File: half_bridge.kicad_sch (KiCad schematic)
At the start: 19 parts

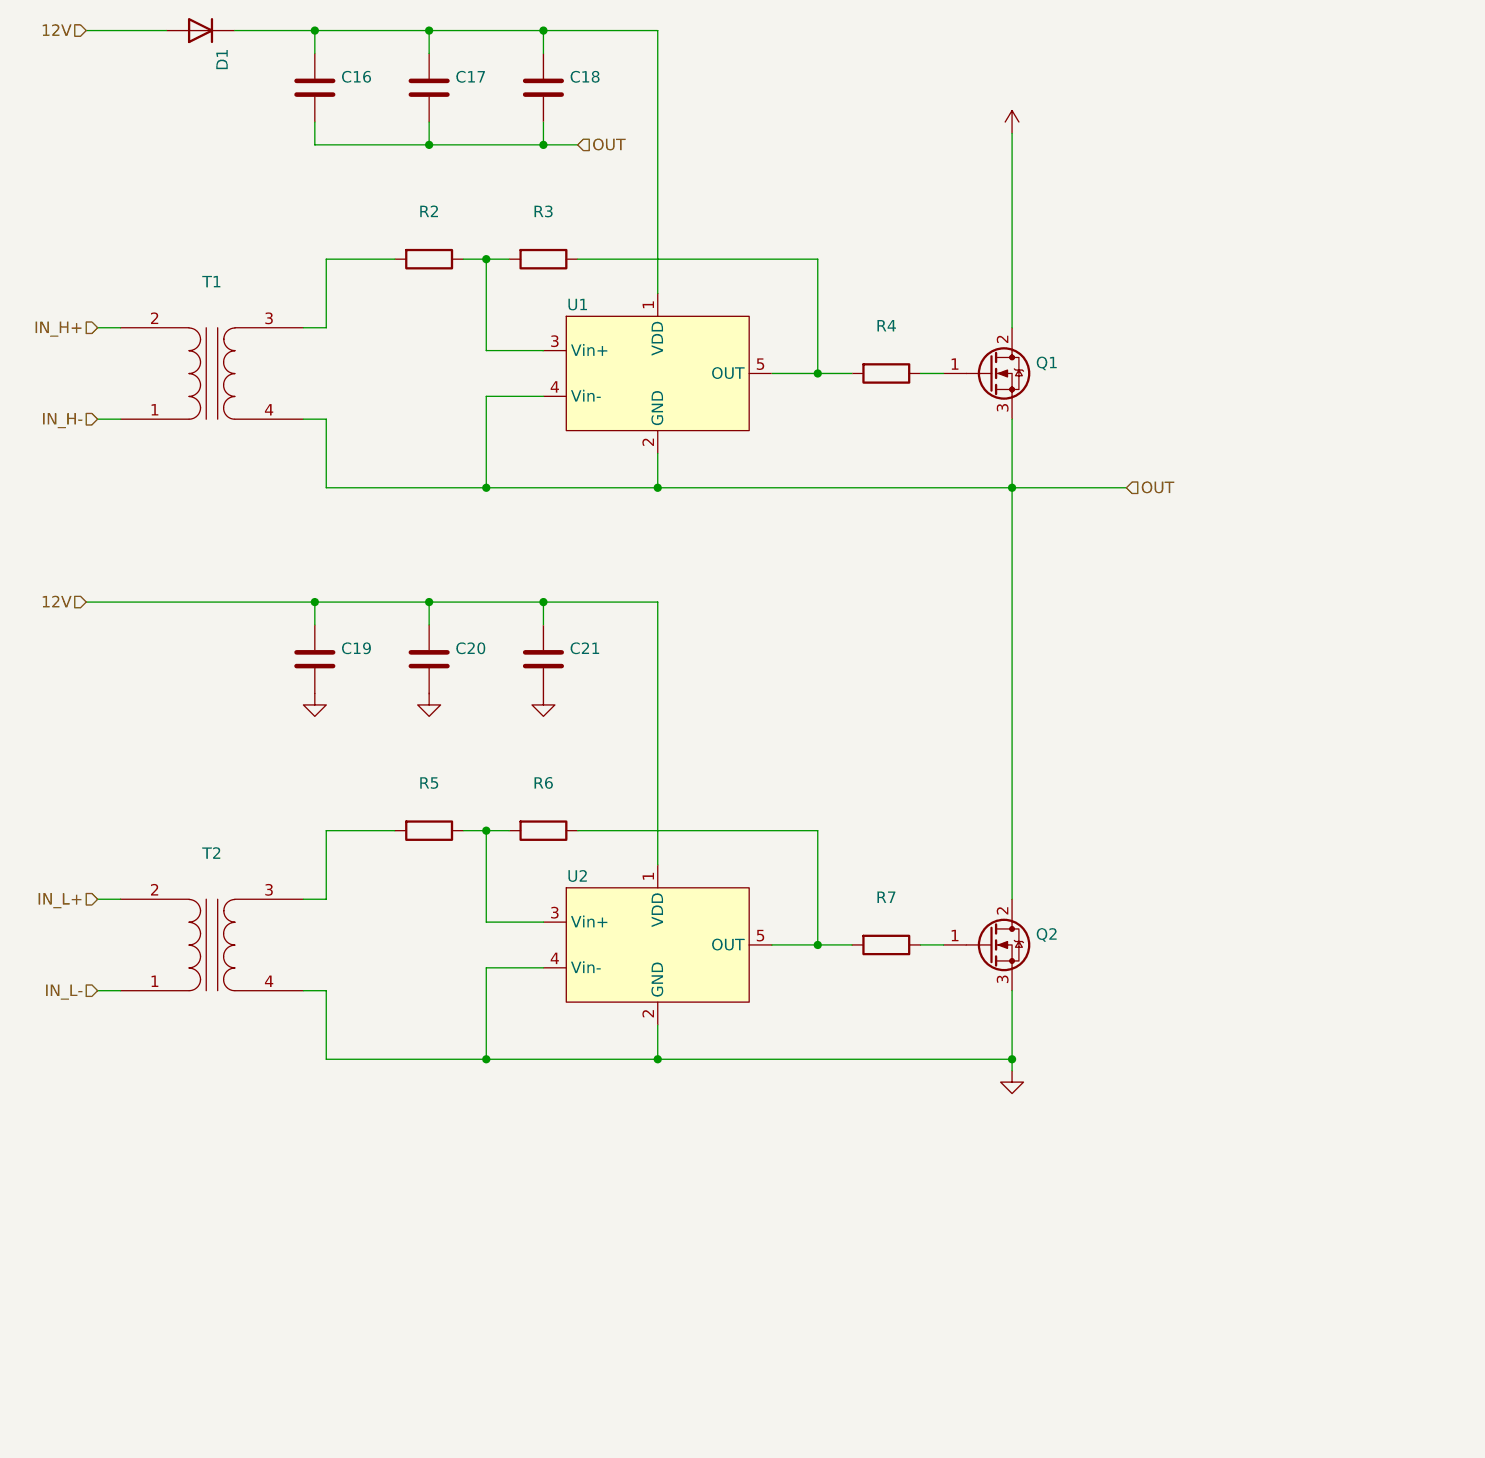
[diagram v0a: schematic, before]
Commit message: added/corrected placeholder resistor values
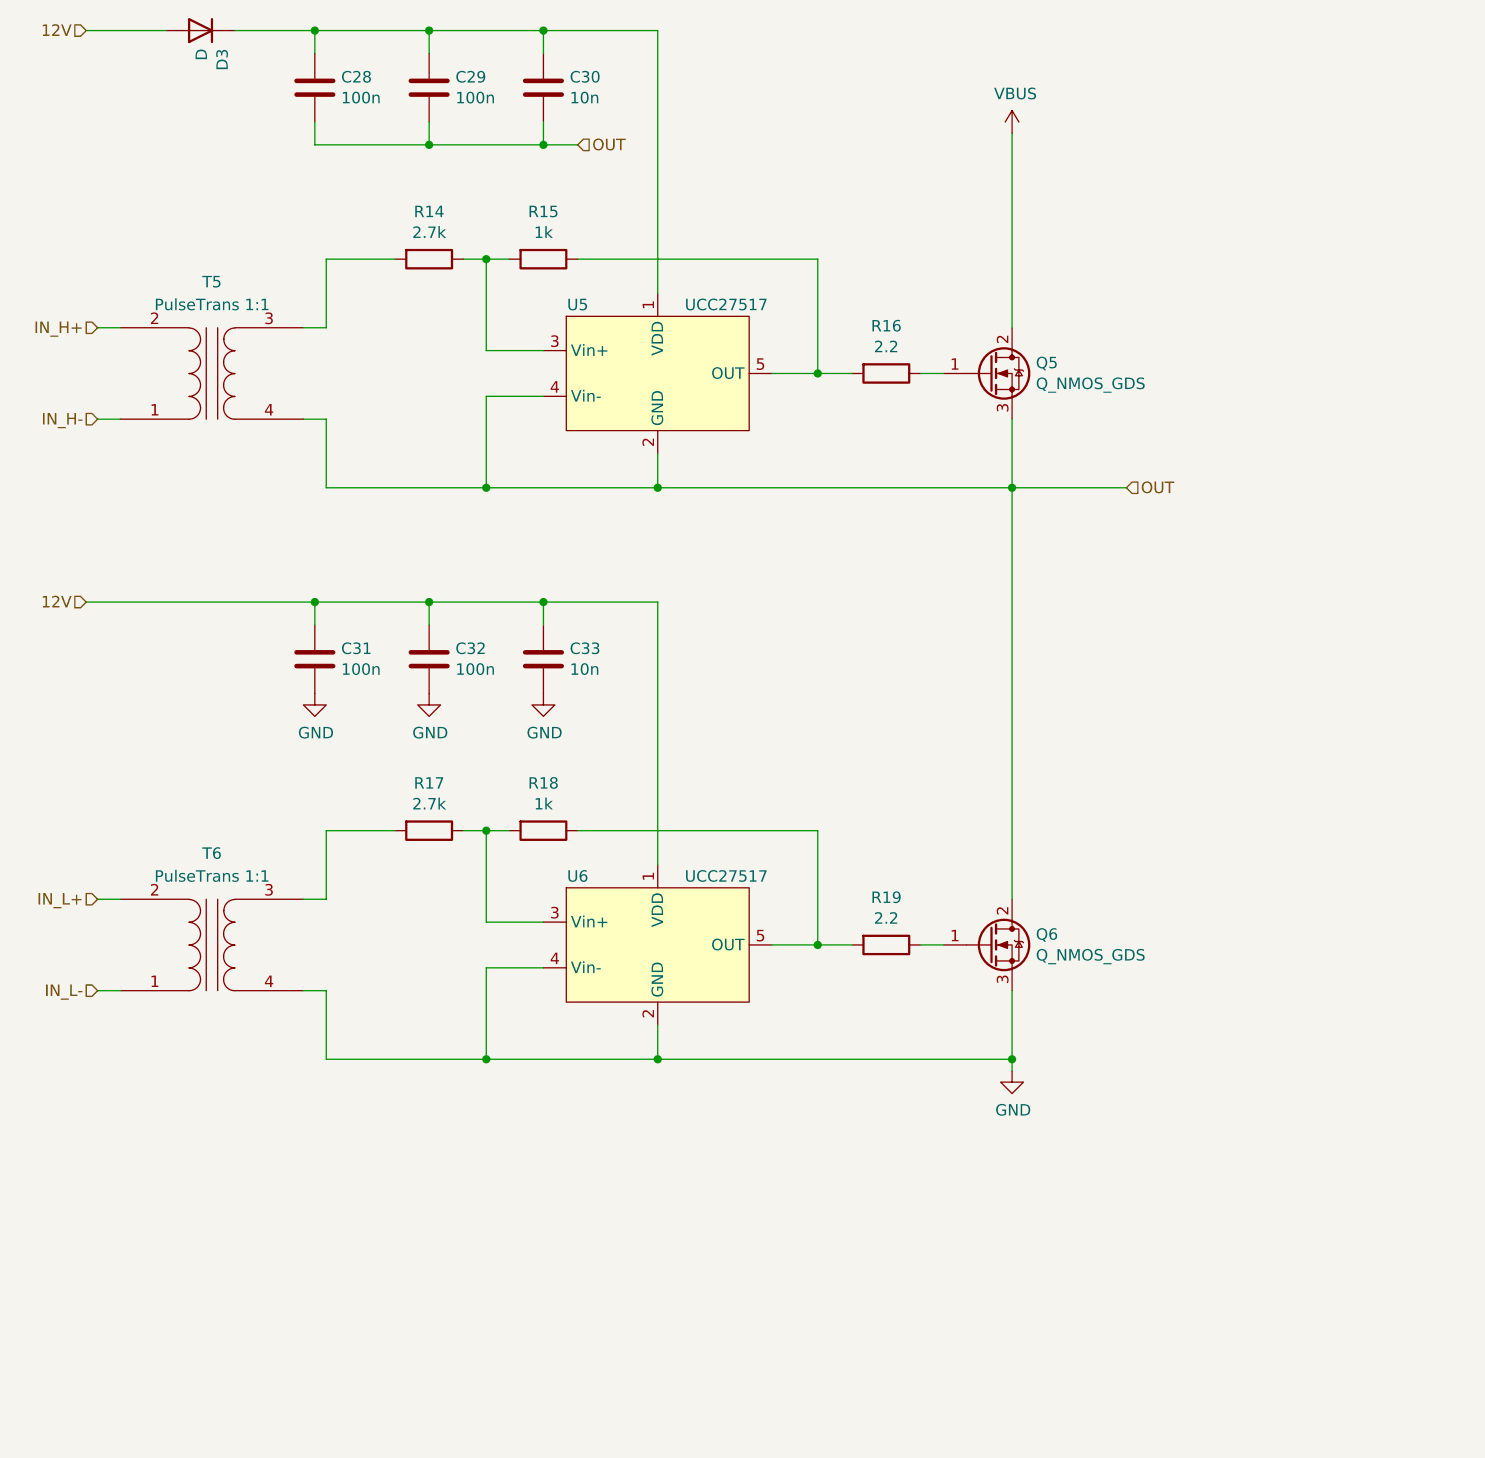
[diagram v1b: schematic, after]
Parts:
- C28: renamed from C16; value (none) -> 100n; footprint (none) -> Capacitor_SMD:C_0603_1608Metric
- C29: renamed from C17; value (none) -> 100n; footprint (none) -> Capacitor_SMD:C_0603_1608Metric
- C30: renamed from C18; value (none) -> 10n; footprint (none) -> Capacitor_SMD:C_0603_1608Metric
- C31: renamed from C19; value (none) -> 100n; footprint (none) -> Capacitor_SMD:C_0603_1608Metric
- C32: renamed from C20; value (none) -> 100n; footprint (none) -> Capacitor_SMD:C_0603_1608Metric
- C33: renamed from C21; value (none) -> 10n; footprint (none) -> Capacitor_SMD:C_0603_1608Metric
- D3: renamed from D1; value (none) -> D; footprint (none) -> Diode_SMD:D_SMA
- Q5: renamed from Q1; value (none) -> Q_NMOS_GDS; footprint (none) -> Package_TO_SOT_THT:TO-247-3_Horizontal_TabUp
- Q6: renamed from Q2; value (none) -> Q_NMOS_GDS; footprint (none) -> Package_TO_SOT_THT:TO-247-3_Horizontal_TabUp
- R14: renamed from R2; value (none) -> 2.7k; footprint (none) -> Resistor_SMD:R_0805_2012Metric
- R15: renamed from R3; value (none) -> 1k; footprint (none) -> Resistor_SMD:R_0805_2012Metric
- R16: renamed from R4; value (none) -> 2.2; footprint (none) -> Resistor_SMD:R_2512_6332Metric_Pad1.40x3.35mm_HandSolder
- R17: renamed from R5; value (none) -> 2.7k; footprint (none) -> Resistor_SMD:R_0805_2012Metric
- R18: renamed from R6; value (none) -> 1k; footprint (none) -> Resistor_SMD:R_0805_2012Metric
- R19: renamed from R7; value (none) -> 2.2; footprint (none) -> Resistor_SMD:R_2512_6332Metric_Pad1.40x3.35mm_HandSolder
- T5: renamed from T1; value (none) -> PulseTrans 1:1; footprint (none) -> universal-half-bridge:ESMIT-4180
- T6: renamed from T2; value (none) -> PulseTrans 1:1; footprint (none) -> universal-half-bridge:ESMIT-4180
- U5: renamed from U1; value (none) -> UCC27517; footprint (none) -> Package_TO_SOT_SMD:SOT-23-5
- U6: renamed from U2; value (none) -> UCC27517; footprint (none) -> Package_TO_SOT_SMD:SOT-23-5

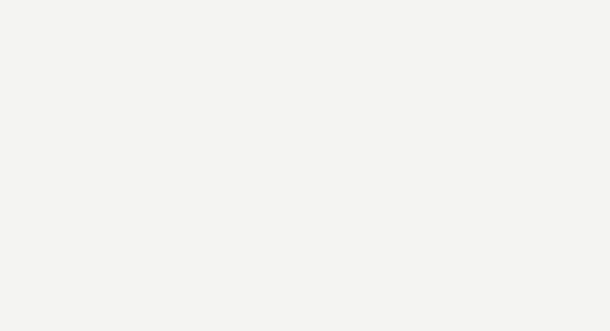
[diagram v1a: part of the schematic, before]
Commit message: added infomation to title block, generated PDF of schematic
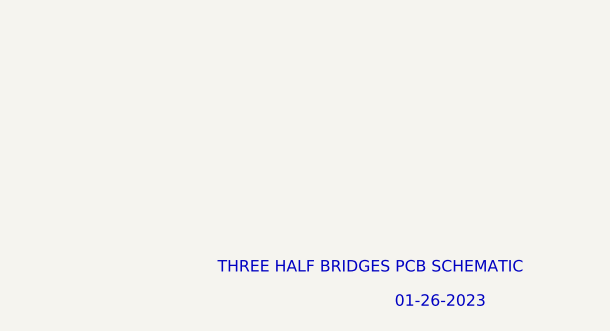
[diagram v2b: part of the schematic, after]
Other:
- note added: "01-26-2023"
- note added: "THREE HALF BRIDGES PCB SCHEMATIC"
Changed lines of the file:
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@@
     (stroke (width 0) (type default) (color 0 0 0 0))
+  )
+  (text "THREE HALF BRIDGES PCB SCHEMATIC" (at 186.69 190.5 0)
+    (effects (font (size 1.27 1.27)) (justify left bottom))
+  )
+  (text "01-26-2023" (at 206.375 194.31 0)
+    (effects (font (size 1.27 1.27)) (justify left bottom))
   )
   (hierarchical_label "12V" (shape input) (at 74.93 101.6 180)
